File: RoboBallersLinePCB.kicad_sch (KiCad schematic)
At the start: 102 parts, among them U1 MCP3008, U2 MCP3008, U3 MCP3008

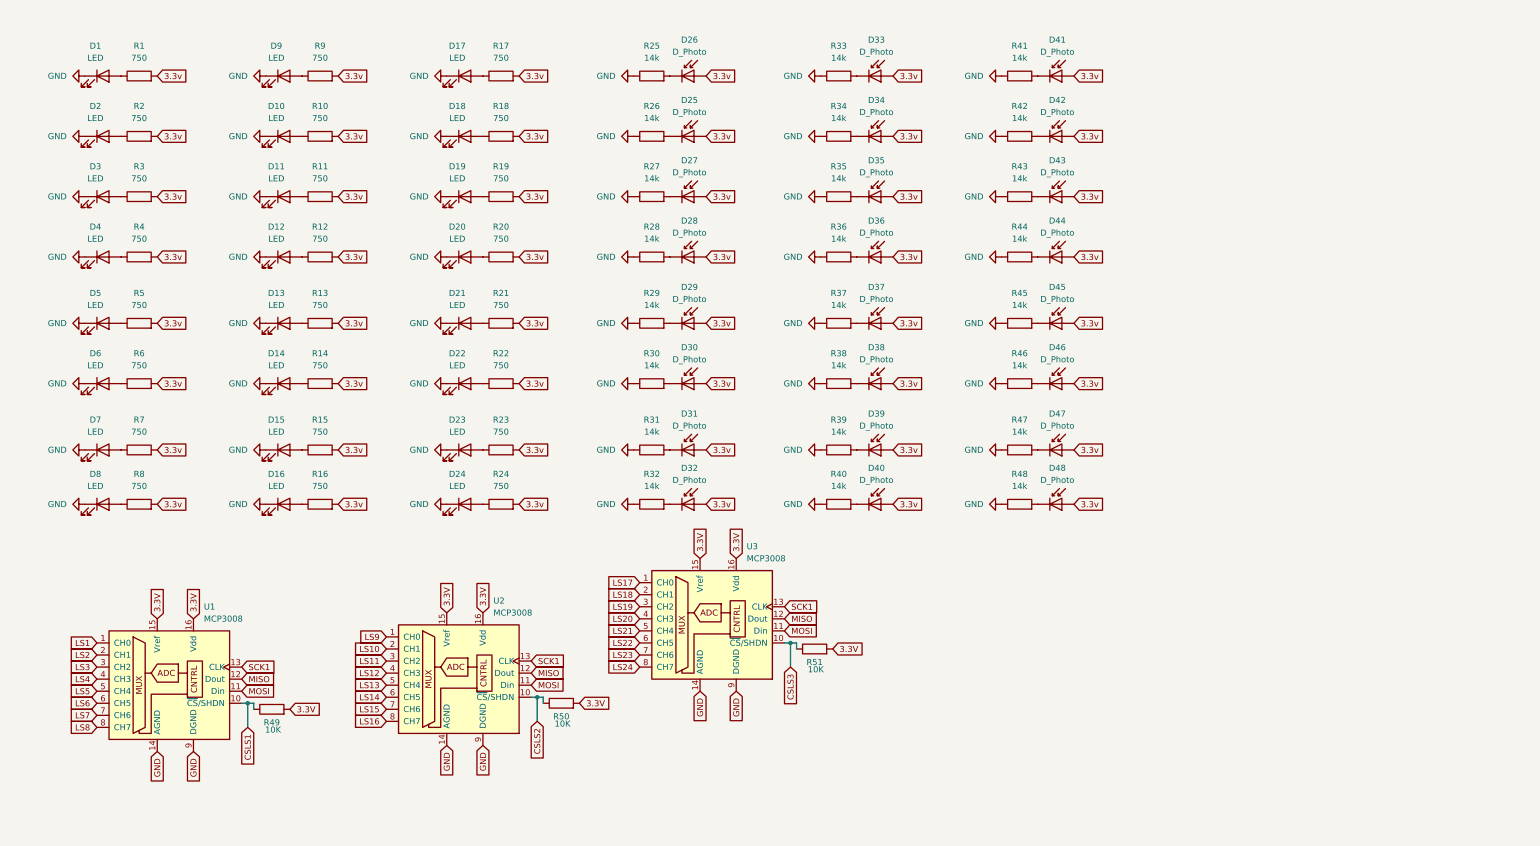
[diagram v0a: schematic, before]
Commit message: Footprints assigned
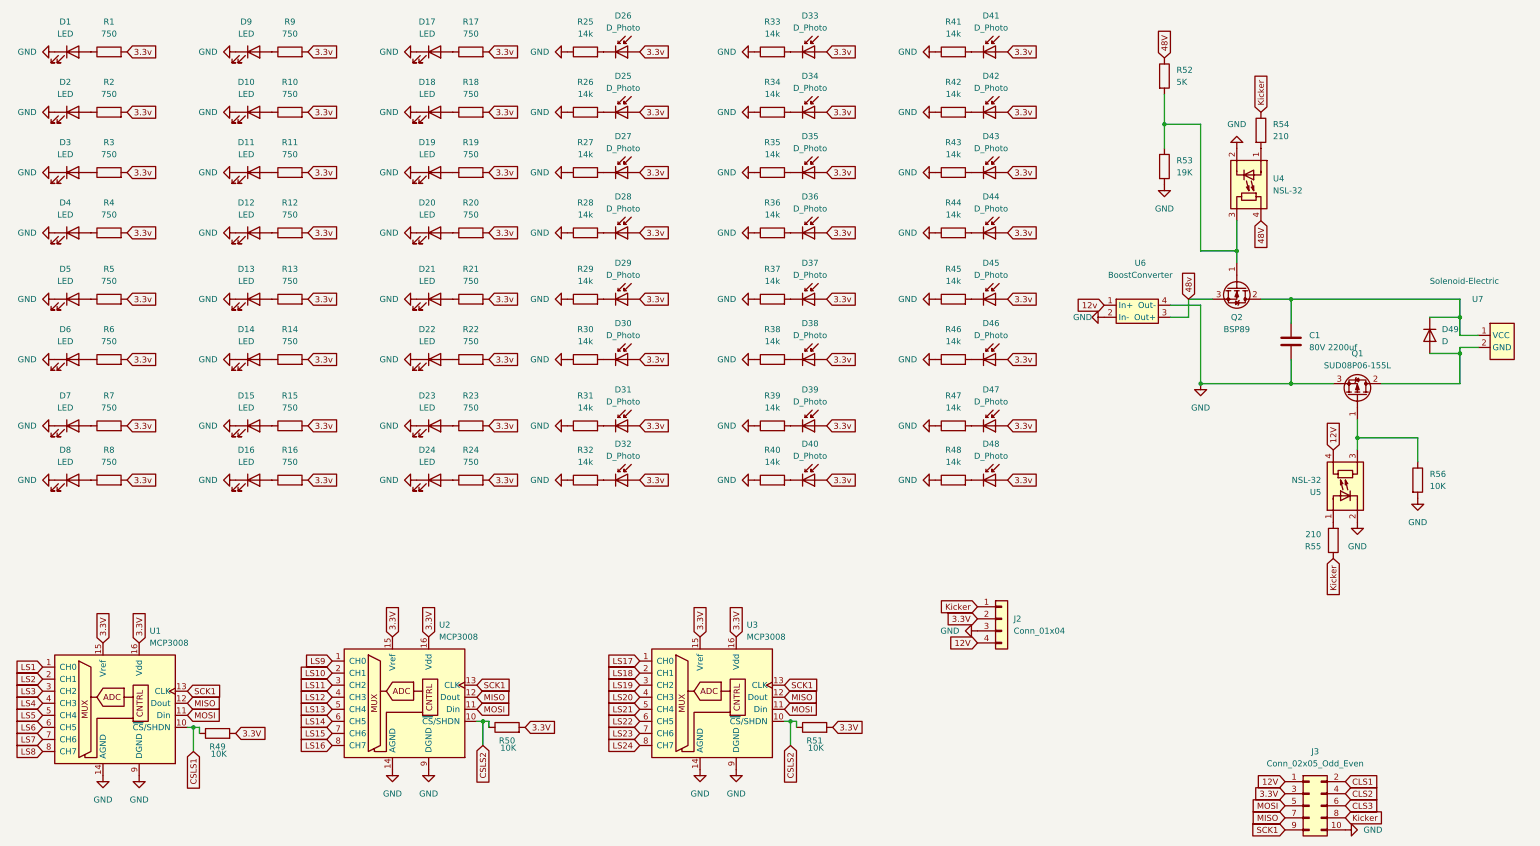
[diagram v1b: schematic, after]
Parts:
- added C1: 80V 2200uf, Capacitor_THT:CP_Radial_D25.0mm_P10.00mm_SnapIn, symbol Device:C
- added D49: D, Diode_THT:D_DO-201AD_P12.70mm_Horizontal, symbol Device:D
- added J2: Conn_01x04, Connector_PinHeader_2.54mm:PinHeader_1x04_P2.54mm_Vertical, symbol Connector_Generic:Conn_01x04
- added J3: Conn_02x05_Odd_Even, Connector_PinHeader_2.54mm:PinHeader_2x05_P2.54mm_Vertical, symbol Connector_Generic:Conn_02x05_Odd_Even
- added Q1: SUD08P06-155L, Package_TO_SOT_SMD:TO-252-2, symbol Transistor_FET:SUD08P06-155L
- added Q2: BSP89, Package_TO_SOT_SMD:SOT-223-3_TabPin2, symbol Transistor_FET:BSP89
- added R52: 5K, Resistor_SMD:R_0805_2012Metric_Pad1.20x1.40mm_HandSolder, symbol Device:R
- added R53: 19K, Resistor_SMD:R_1206_3216Metric_Pad1.30x1.75mm_HandSolder, symbol Device:R
- added R54, R55: 210, Resistor_SMD:R_1206_3216Metric_Pad1.30x1.75mm_HandSolder, symbol Device:R
- added R56: 10K, Resistor_THT:R_Axial_DIN0204_L3.6mm_D1.6mm_P7.62mm_Horizontal, symbol Device:R
- added U4, U5: NSL-32, OptoDevice:Luna_NSL-32, symbol Isolator:NSL-32
- added U6: BoostConverter, Connector_PinHeader_2.54mm:PinHeader_2x05_P2.54mm_Vertical, symbol BoostConverter:BoostConverter
- added U7: Solenoid-Electric, Connector_PinSocket_2.54mm:PinSocket_1x02_P2.54mm_Vertical, symbol Solenoid:Solenoid-Electric
- D25, D26, D27, D28, D29, D30, D31, D32, D33, D34, D35, D36, D37, D38, D39, D40, D41, D42, D43, D44, D45, D46, D47, D48: footprint (none) -> LED_SMD:LED_0805_2012Metric_Pad1.15x1.40mm_HandSolder
- R25, R26, R27, R28, R29, R30, R31, R32, R33, R34, R35, R36, R37, R38, R39, R40, R41, R42, R43, R44, R45, R46, R47, R48: footprint (none) -> Resistor_SMD:R_1210_3225Metric_Pad1.30x2.65mm_HandSolder
- R49, R50, R51: footprint (none) -> Resistor_THT:R_Axial_DIN0204_L3.6mm_D1.6mm_P7.62mm_Horizontal
- U1, U2, U3: footprint (none) -> digikey-footprints:DIP-16_W7.62mm
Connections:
- net CSLS3 is gone; now on net CSLS2: R51.1, U3.10 (~{CS}/SHDN)
- net 3.3V: now also J2.2 (Pin_2), J3.3 (Pin_3)
- net GND: now also C1.2, J2.3 (Pin_3), J3.10 (Pin_10), Q1.3 (S), R53.2, R56.2, U4.2 (K), U5.2 (K), U6.2 (In-), U6.4 (Out-)
- net MISO: now also J3.7 (Pin_7)
- net MOSI: now also J3.5 (Pin_5)
- net SCK1: now also J3.9 (Pin_9)
- new net: C1.1, D49.1 (K), Q2.2 (D), U7.1 (VCC)
- new net: D49.2 (A), Q1.2 (D), U7.2 (GND)
- new net: Q2.1 (G), R52.2, R53.1, U4.3 (R)
- new net: R54.2, U4.1 (A)
- new net: R55.2, U5.1 (A)
- new net: Q1.1 (G), R56.1, U5.3 (R)
- new net 12V: J2.4 (Pin_4), J3.1 (Pin_1), U5.4 (R)
- new net 12v: U6.1 (In+)
- new net 48V: R52.1, U4.4 (R)
- new net 48v: Q2.3 (S), U6.3 (Out+)
- new net CLS1: J3.2 (Pin_2)
- new net CLS2: J3.4 (Pin_4)
- new net CLS3: J3.6 (Pin_6)
- new net Kicker: J2.1 (Pin_1), J3.8 (Pin_8), R54.1, R55.1
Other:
- moved on the sheet: D1, D10, D11, D12, D13, D14, D15, D16, D17, D18, D19, D2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

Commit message: added stuff
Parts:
- U6: footprint Connector_PinHeader_2.54mm:PinHeader_2x05_P2.54mm_Vertical -> Boost Converter:Boost_Convertor_LM2577
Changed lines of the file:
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@@
 			)
 		)
-		(property "Footprint" "Connector_PinHeader_2.54mm:PinHeader_2x05_P2.54mm_Vertical"
+		(property "Footprint" "Boost Converter:Boost_Convertor_LM2577"
 			(at 248.92 76.2 0)
 			(effects
